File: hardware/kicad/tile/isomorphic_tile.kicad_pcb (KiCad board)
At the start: 2 copper layers, 97 x 109 mm, 135 parts, among them J101 Conn_LEFT, J102 Conn_TOP, J103 Conn_BOTTOM, J104 Conn_RIGHT, J105 BTNs_L_MSB, J106 BTNs_L_LSB, J107 BTNs_MSB, J108 BTNs_LSB, SW101 SW_Push, SW102 SW_Push, SW103 SW_Push, SW104 SW_Push, SW105 SW_Push, SW106 SW_Push, SW107 SW_Push, SW108 SW_Push, SW109 SW_Push, SW110 SW_Push, SW111 SW_Push, SW112 SW_Push, U101 74AUC2G126, U102 74AUC2G08, U103 74HC165, U104 74HC165, U105 74AHC1G04, U106 74LVC2G32, U107 74AUC2G125, U108 74LVC2G74, U109 74LS161

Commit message: KiCad: rename Italian field and footprint names
- Symbol field "Codice" (manufacturer part number) -> "MPN".
- Mouse-bite footprint "Senza-titolo" -> "MouseBite_NPTH_0.5mm".

Verified: netlist identical to rev A, switch/connector/outline
invariants OK, DRC report counts unchanged.
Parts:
- REF**10 (x4), REF**11 (x4), REF**12 (x4), REF**13 (x4), REF**14 (x4), REF**15 (x4), REF**16 (x4), REF**17 (x4), REF**18 (x4), REF**19 (x3), REF**2, REF**3 (x4), REF**4 (x4), REF**5 (x4), REF**6 (x4), REF**7 (x4), REF**8 (x4), REF**9 (x4): footprint Senza-titolo -> MouseBite_NPTH_0.5mm
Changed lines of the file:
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@@
 	(net 67 "GND_T")
 	(net 68 "VCC_T")
-	(footprint "Senza-titolo"
+	(footprint "MouseBite_NPTH_0.5mm"
 		(layer "F.Cu")
 		(at 167.9 95.75)
@@
 		(embedded_fonts no)
 	)
-	(footprint "Senza-titolo"
+	(footprint "MouseBite_NPTH_0.5mm"
 		(layer "F.Cu")
 		(at 169.5 95.75)
@@
 		(embedded_fonts no)
 	)
-	(footprint "Senza-titolo"
+	(footprint "MouseBite_NPTH_0.5mm"
 		(layer "F.Cu")
 		(at 121.3 95.75)
@@
 		(embedded_fonts no)
 	)
-	(footprint "Senza-titolo"
+	(footprint "MouseBite_NPTH_0.5mm"
 		(layer "F.Cu")
 		(at 172.9 109)
@@
 		(embedded_fonts no)
 	)
-	(footprint "Senza-titolo"
+	(footprint "MouseBite_NPTH_0.5mm"
 		(layer "F.Cu")
 		(at 170.3 95.75)
@@
 		(embedded_fonts no)
 	)
-	(footprint "Senza-titolo"
+	(footprint "MouseBite_NPTH_0.5mm"
 		(layer "F.Cu")
 		(at 172.1 109)
@@
 		(embedded_fonts no)
 	)
-	(footprint "Senza-titolo"
+	(footprint "MouseBite_NPTH_0.5mm"
 		(layer "F.Cu")
 		(at 123.7 95.75)
@@
 		)
 	)
-	(footprint "Senza-titolo"
+	(footprint "MouseBite_NPTH_0.5mm"
 		(layer "F.Cu")
 		(at 126.1 95.75)
@@
 		(embedded_fonts no)
 	)
-	(footprint "Senza-titolo"
+	(footprint "MouseBite_NPTH_0.5mm"
 		(layer "F.Cu")
 		(at 124.5 95.75)
@@
 		(embedded_fonts no)
 	)
-	(footprint "Senza-titolo"
+	(footprint "MouseBite_NPTH_0.5mm"
 		(layer "F.Cu")
 		(at 131 109)
@@
 		(embedded_fonts no)
 	)
-	(footprint "Senza-titolo"
+	(footprint "MouseBite_NPTH_0.5mm"
 		(layer "F.Cu")
 		(at 159.9 95.75)
@@
 		)
 	)
-	(footprint "Senza-titolo"
+	(footprint "MouseBite_NPTH_0.5mm"
 		(layer "F.Cu")
 		(at 128.5 95.75)
@@
 		(embedded_fonts no)
 	)
-	(footprint "Senza-titolo"
+	(footprint "MouseBite_NPTH_0.5mm"
 		(layer "F.Cu")
 		(at 164.7 95.75)
@@
 		)
 	)
-	(footprint "Senza-titolo"
+	(footprint "MouseBite_NPTH_0.5mm"
 		(layer "F.Cu")
 		(at 163.9 95.75)
@@
 		(embedded_fonts no)
 	)
-	(footprint "Senza-titolo"
+	(footprint "MouseBite_NPTH_0.5mm"
 		(layer "F.Cu")
 		(at 127.7 95.75)
@@
 		(embedded_fonts no)
 	)
-	(footprint "Senza-titolo"
+	(footprint "MouseBite_NPTH_0.5mm"
 		(layer "F.Cu")
 		(at 125.3 95.75)
@@
 		(embedded_fonts no)
 	)
-	(footprint "Senza-titolo"
+	(footprint "MouseBite_NPTH_0.5mm"
 		(layer "F.Cu")
 		(at 122.1 95.75)
@@
 		)
 	)
-	(footprint "Senza-titolo"
+	(footprint "MouseBite_NPTH_0.5mm"
 		(layer "F.Cu")
 		(at 162.5 109)
@@
 		)
 	)
-	(footprint "Senza-titolo"
+	(footprint "MouseBite_NPTH_0.5mm"
 		(layer "F.Cu")
 		(at 168.9 109)
@@
 		)
 	)
-	(footprint "Senza-titolo"
+	(footprint "MouseBite_NPTH_0.5mm"
 		(layer "F.Cu")
 		(at 165.7 109)
@@
 		(embedded_fonts no)
 	)
-	(footprint "Senza-titolo"
+	(footprint "MouseBite_NPTH_0.5mm"
 		(layer "F.Cu")
 		(at 118.9 95.75)
@@
 		)
 	)
-	(footprint "Senza-titolo"
+	(footprint "MouseBite_NPTH_0.5mm"
 		(layer "F.Cu")
 		(at 126.2 109)
@@
 		)
 	)
-	(footprint "Senza-titolo"
+	(footprint "MouseBite_NPTH_0.5mm"
 		(layer "F.Cu")
 		(at 160.1 109)
@@
 		(embedded_fonts no)
 	)
-	(footprint "Senza-titolo"
+	(footprint "MouseBite_NPTH_0.5mm"
 		(layer "F.Cu")
 		(at 127 109)
@@
 		(embedded_fonts no)
 	)
-	(footprint "Senza-titolo"
+	(footprint "MouseBite_NPTH_0.5mm"
 		(layer "F.Cu")
 		(at 129.3 95.75)
@@
 		)
 	)
-	(footprint "Senza-titolo"
+	(footprint "MouseBite_NPTH_0.5mm"
 		(layer "F.Cu")
 		(at 166.3 95.75)
@@
 		(embedded_fonts no)
 	)
-	(footprint "Senza-titolo"
+	(footprint "MouseBite_NPTH_0.5mm"
 		(layer "F.Cu")
 		(at 123.8 109)
@@
 		(embedded_fonts no)
 	)
-	(footprint "Senza-titolo"
+	(footprint "MouseBite_NPTH_0.5mm"
 		(layer "F.Cu")
 		(at 121.4 109)
@@
 		(embedded_fonts no)
 	)
-	(footprint "Senza-titolo"
+	(footprint "MouseBite_NPTH_0.5mm"
 		(layer "F.Cu")
 		(at 171.3 109)
@@
 		(embedded_fonts no)
 	)
-	(footprint "Senza-titolo"
+	(footprint "MouseBite_NPTH_0.5mm"
 		(layer "F.Cu")
 		(at 168.1 109)
@@
 		(embedded_fonts no)
 	)
-	(footprint "Senza-titolo"
+	(footprint "MouseBite_NPTH_0.5mm"
 		(layer "F.Cu")
 		(at 119.7 95.75)
@@
 		)
 	)
-	(footprint "Senza-titolo"
+	(footprint "MouseBite_NPTH_0.5mm"
 		(layer "F.Cu")
 		(at 131.8 109)
@@
 		)
 	)
-	(footprint "Senza-titolo"
+	(footprint "MouseBite_NPTH_0.5mm"
 		(layer "F.Cu")
 		(at 171.1 95.75)
@@
 		)
 	)
-	(footprint "Senza-titolo"
+	(footprint "MouseBite_NPTH_0.5mm"
 		(layer "F.Cu")
 		(at 167.3 109)
@@
 		(embedded_fonts no)
 	)
-	(footprint "Senza-titolo"
+	(footprint "MouseBite_NPTH_0.5mm"
 		(layer "F.Cu")
 		(at 122.2 109)
@@
 		)
 	)
-	(footprint "Senza-titolo"
+	(footprint "MouseBite_NPTH_0.5mm"
 		(layer "F.Cu")
 		(at 119.8 109)
@@
 		(embedded_fonts no)
 	)
-	(footprint "Senza-titolo"
+	(footprint "MouseBite_NPTH_0.5mm"
 		(layer "F.Cu")
 		(at 166.5 109)
@@
 		(embedded_fonts no)
 	)
-	(footprint "Senza-titolo"
+	(footprint "MouseBite_NPTH_0.5mm"
 		(layer "F.Cu")
 		(at 129.4 109)
@@
 		)
 	)
-	(footprint "Senza-titolo"
+	(footprint "MouseBite_NPTH_0.5mm"
 		(layer "F.Cu")
 		(at 123 109)
@@
 		)
 	)
-	(footprint "Senza-titolo"
+	(footprint "MouseBite_NPTH_0.5mm"
 		(layer "F.Cu")
 		(at 124.6 109)
@@
 		)
 	)
-	(footprint "Senza-titolo"
+	(footprint "MouseBite_NPTH_0.5mm"
 		(layer "F.Cu")
 		(at 164.1 109)
@@
 		(embedded_fonts no)
 	)
-	(footprint "Senza-titolo"
+	(footprint "MouseBite_NPTH_0.5mm"
 		(layer "F.Cu")
 		(at 162.3 95.75)
@@
 		)
 	)
-	(footprint "Senza-titolo"
+	(footprint "MouseBite_NPTH_0.5mm"
 		(layer "F.Cu")
 		(at 165.5 95.75)
@@
 		(embedded_fonts no)
 	)
-	(footprint "Senza-titolo"
+	(footprint "MouseBite_NPTH_0.5mm"
 		(layer "F.Cu")
 		(at 126.9 95.75)
@@
 		(embedded_fonts no)
 	)
-	(footprint "Senza-titolo"
+	(footprint "MouseBite_NPTH_0.5mm"
 		(layer "F.Cu")
 		(at 120.6 109)
@@
 		)
 	)
-	(footprint "Senza-titolo"
+	(footprint "MouseBite_NPTH_0.5mm"
 		(layer "F.Cu")
 		(at 160.7 95.75)
@@
 		)
 	)
-	(footprint "Senza-titolo"
+	(footprint "MouseBite_NPTH_0.5mm"
 		(layer "F.Cu")
 		(at 161.7 109)
@@
 		)
 	)
-	(footprint "Senza-titolo"
+	(footprint "MouseBite_NPTH_0.5mm"
 		(layer "F.Cu")
 		(at 172.7 95.75)
@@
 		(embedded_fonts no)
 	)
-	(footprint "Senza-titolo"
+	(footprint "MouseBite_NPTH_0.5mm"
 		(layer "F.Cu")
 		(at 125.4 109)
@@
 		(embedded_fonts no)
 	)
-	(footprint "Senza-titolo"
+	(footprint "MouseBite_NPTH_0.5mm"
 		(layer "F.Cu")
 		(at 167.1 95.75)
@@
 		(embedded_fonts no)
 	)
-	(footprint "Senza-titolo"
+	(footprint "MouseBite_NPTH_0.5mm"
 		(layer "F.Cu")
 		(at 171.9 95.75)
@@
 		)
 	)
-	(footprint "Senza-titolo"
+	(footprint "MouseBite_NPTH_0.5mm"
 		(layer "F.Cu")
 		(at 170.5 109)
@@
 		)
 	)
-	(footprint "Senza-titolo"
+	(footprint "MouseBite_NPTH_0.5mm"
 		(layer "F.Cu")
 		(at 131.7 95.75)
@@
 		(embedded_fonts no)
 	)
-	(footprint "Senza-titolo"
+	(footprint "MouseBite_NPTH_0.5mm"
 		(layer "F.Cu")
 		(at 120.5 95.75)
@@
 		)
 	)
-	(footprint "Senza-titolo"
+	(footprint "MouseBite_NPTH_0.5mm"
 		(layer "F.Cu")
 		(at 164.9 109)
@@
 		(embedded_fonts no)
 	)
-	(footprint "Senza-titolo"
+	(footprint "MouseBite_NPTH_0.5mm"
 		(layer "F.Cu")
 		(at 169.7 109)
@@
 		)
 	)
-	(footprint "Senza-titolo"
+	(footprint "MouseBite_NPTH_0.5mm"
 		(layer "F.Cu")
 		(at 127.8 109)
@@
 		)
 	)
-	(footprint "Senza-titolo"
+	(footprint "MouseBite_NPTH_0.5mm"
 		(layer "F.Cu")
 		(at 122.9 95.75)
@@
 		)
 	)
-	(footprint "Senza-titolo"
+	(footprint "MouseBite_NPTH_0.5mm"
 		(layer "F.Cu")
 		(at 119 109)
@@
 		(embedded_fonts no)
 	)
-	(footprint "Senza-titolo"
+	(footprint "MouseBite_NPTH_0.5mm"
 		(layer "F.Cu")
 		(at 130.2 109)
@@
 		)
 	)
-	(footprint "Senza-titolo"
+	(footprint "MouseBite_NPTH_0.5mm"
 		(layer "F.Cu")
 		(at 130.1 95.75)
@@
 		)
 	)
-	(footprint "Senza-titolo"
+	(footprint "MouseBite_NPTH_0.5mm"
 		(layer "F.Cu")
 		(at 130.9 95.75)
@@
 		(embedded_fonts no)
 	)
-	(footprint "Senza-titolo"
+	(footprint "MouseBite_NPTH_0.5mm"
 		(layer "F.Cu")
 		(at 163.1 95.75)
@@
 		(embedded_fonts no)
 	)
-	(footprint "Senza-titolo"
+	(footprint "MouseBite_NPTH_0.5mm"
 		(layer "F.Cu")
 		(at 128.6 109)
@@
 		(embedded_fonts no)
 	)
-	(footprint "Senza-titolo"
+	(footprint "MouseBite_NPTH_0.5mm"
 		(layer "F.Cu")
 		(at 168.7 95.75)
@@
 		(embedded_fonts no)
 	)
-	(footprint "Senza-titolo"
+	(footprint "MouseBite_NPTH_0.5mm"
 		(layer "F.Cu")
 		(at 163.3 109)
@@
 		(embedded_fonts no)
 	)
-	(footprint "Senza-titolo"
+	(footprint "MouseBite_NPTH_0.5mm"
 		(layer "F.Cu")
 		(at 160.9 109)
@@
 		)
 	)
-	(footprint "Senza-titolo"
+	(footprint "MouseBite_NPTH_0.5mm"
 		(layer "F.Cu")
 		(at 161.5 95.75)

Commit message: Rev B PCB: 4 layers, single-sided assembly, hot-swap sockets
Produced by hardware/kicad/tile/scripts/revb_pcb.py and
revb_pipeline.sh (rev-A board -> netlist update -> placement ->
Freerouting -> stitching/pours), fully reproducible.

- 4-layer 1.6 mm stack-up, In1 GND/GND_T and In2 VCC/VCC_T planes,
  Interboard net class 0.3 mm (~55 ohm), 4 mm ground stitching grid.
- Key board: Kailh MX hot-swap sockets and all resistors on B.Cu;
  switch centres unchanged (edge-trimmed socket footprint variant for
  the switches next to the stepped outline).
- Logic board: every SMD part on F.Cu; series resistors within 2.6 mm
  of their drivers; one 100 nF next to each IC.
- Fiducials (3 per board), board-only mouse bites, silkscreen revision
  v0.2, J107 courtyard margin reduced towards the SW111 socket.

Verified: DRC 0 errors, 0 unconnected, 0 schematic-parity issues;
switch/connector/outline invariants OK; SPICE tile hop as routed:
1 % overshoot (rev A: 22 %).
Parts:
- added C201: 100n, Capacitor_SMD:C_0603_1608Metric, F.Cu at (120.6, 116.8)
- added C202: 100n, Capacitor_SMD:C_0603_1608Metric, F.Cu at (137.7, 114.3)
- added C203: 100n, Capacitor_SMD:C_0603_1608Metric, F.Cu at (148.1, 119.0)
- added C204: 100n, Capacitor_SMD:C_0603_1608Metric, F.Cu at (129.3, 137.9)
- added C205: 100n, Capacitor_SMD:C_0603_1608Metric, F.Cu at (119.6, 140.3)
- added C206: 100n, Capacitor_SMD:C_0603_1608Metric, F.Cu at (133.7, 137.0)
- added C207: 100n, Capacitor_SMD:C_0603_1608Metric, F.Cu at (154.7, 130.0)
- added C208: 100n, Capacitor_SMD:C_0603_1608Metric, F.Cu at (139.6, 122.8)
- added C209: 100n, Capacitor_SMD:C_0603_1608Metric, F.Cu at (150.1, 142.8)
- added FID1: Fiducial, Fiducial:Fiducial_1mm_Mask2mm, B.Cu at (119.5, 73.2)
- added FID2: Fiducial, Fiducial:Fiducial_1mm_Mask2mm, B.Cu at (201.5, 56.0)
- added FID3: Fiducial, Fiducial:Fiducial_1mm_Mask2mm, B.Cu at (110.5, 93.0)
- added FID4: Fiducial, Fiducial:Fiducial_1mm_Mask2mm, F.Cu at (112.0, 151.0)
- added FID5: Fiducial, Fiducial:Fiducial_1mm_Mask2mm, F.Cu at (179.0, 151.0)
- added FID6: Fiducial, Fiducial:Fiducial_1mm_Mask2mm, F.Cu at (179.0, 112.0)
- added R201: 33, Resistor_SMD:R_0603_1608Metric, F.Cu at (124.1, 118.5)
- added R202: 33, Resistor_SMD:R_0603_1608Metric, F.Cu at (157.2, 127.6)
- added R203: 33, Resistor_SMD:R_0603_1608Metric, F.Cu at (133.9, 133.6)
- added R204: 33, Resistor_SMD:R_0603_1608Metric, F.Cu at (136.2, 136.1)
- added R205: 33, Resistor_SMD:R_0603_1608Metric, F.Cu at (140.2, 140.2)
- added R206: 33, Resistor_SMD:R_0603_1608Metric, F.Cu at (137.7, 137.9)
- added R207: 33, Resistor_SMD:R_0603_1608Metric, F.Cu at (139.6, 128.2)
- C101, C102: footprint Capacitor_SMD:C_0805_2012Metric_Pad1.18x1.45mm_HandSolder -> Capacitor_SMD:C_0603_1608Metric; moved to F.Cu
- C103, C104: footprint Capacitor_SMD:C_1206_3216Metric_Pad1.33x1.80mm_HandSolder -> Capacitor_SMD:C_1206_3216Metric
- C105: footprint Capacitor_THT:CP_Radial_D6.3mm_P2.50mm -> Capacitor_SMD:CP_Elec_6.3x7.7
- R101, R108: footprint Resistor_SMD:R_0805_2012Metric_Pad1.20x1.40mm_HandSolder -> Resistor_SMD:R_0603_1608Metric; moved to F.Cu
- R102, R103, R104, R105, R106, R107, R109: footprint Resistor_SMD:R_0805_2012Metric_Pad1.20x1.40mm_HandSolder -> Resistor_SMD:R_0603_1608Metric
- R110, R111, R112, R113, R114, R115, R116, R117, R118, R119, R120, R121: value 100R -> 100; footprint Resistor_SMD:R_0805_2012Metric_Pad1.20x1.40mm_HandSolder -> Resistor_SMD:R_0603_1608Metric
- R122, R123, R124, R125, R126, R127, R128, R129, R130, R131, R132, R133: footprint Resistor_SMD:R_0805_2012Metric_Pad1.20x1.40mm_HandSolder -> Resistor_SMD:R_0603_1608Metric; moved to B.Cu
- SW101, SW102, SW103, SW104, SW105, SW106, SW107, SW108, SW109, SW110, SW111, SW112: footprint Button_Switch_Keyboard:SW_Cherry_MX_1.00u_PCB -> Switch_Keyboard_Hotswap_Kailh:SW_Hotswap_Kailh_MX_1.00u_EdgeTrim
- U101: value 74AUC2G126 -> 74LVC2G126; footprint Package_SO:MSOP-8_3x3mm_P0.65mm -> Package_SO:SSOP-8_2.95x2.8mm_P0.65mm; moved to F.Cu
- U102: value 74AUC2G08 -> 74LVC2G08; footprint Package_SO:MSOP-8_3x3mm_P0.65mm -> Package_SO:SSOP-8_2.95x2.8mm_P0.65mm
- U103: value 74HC165 -> 74LVC165A
- U104: value 74HC165 -> 74LVC165A; moved to F.Cu
- U105: value 74AHC1G04 -> 74LVC1G04; footprint Package_TO_SOT_SMD:SOT-23-5_HandSoldering -> Package_TO_SOT_SMD:SOT-23-5
- U106, U108: footprint Package_SO:MSOP-8_3x3mm_P0.65mm -> Package_SO:SSOP-8_2.95x2.8mm_P0.65mm
- U107: value 74AUC2G125 -> 74LVC2G125; footprint Package_SO:MSOP-8_3x3mm_P0.65mm -> Package_SO:SSOP-8_2.95x2.8mm_P0.65mm; moved to F.Cu
- U109: value 74LS161 -> 74HC161; moved to F.Cu
- moved U104 11.6 mm to (133.8, 142.7), turned to 90 degrees
- moved U109 9.80 mm to (156.5, 145.3), turned to 90 degrees
- moved U103 9.25 mm to (154.5, 121.5), turned to 90 degrees
- moved C105 7.57 mm to (171.8, 139.5)
- moved U107 6.00 mm to (153.2, 127.2), turned to 0 degrees
- moved SW104 5.68 mm to (126.0, 70.4)
- moved SW101 5.68 mm to (155.9, 53.1)
- moved SW102 5.68 mm to (135.9, 53.1)
- moved SW103 5.68 mm to (146.0, 70.4)
- moved SW105 5.68 mm to (135.9, 87.7)
- moved SW107 5.68 mm to (195.9, 53.1)
- moved SW108 5.68 mm to (175.9, 53.1)
- moved SW109 5.68 mm to (186.0, 70.4)
- moved SW110 5.68 mm to (166.0, 70.4)
- moved SW112 5.68 mm to (155.9, 87.7)
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- renumbered REF**13 to MB1, REF**18 to MB10, REF**3 to MB11, REF**15 to MB12, REF**9 to MB13, REF**8 to MB14, REF**14 to MB15, REF**11 to MB16, REF**7 to MB17, REF**5 to MB18, REF**13 to MB19, REF**15 to MB2, REF**9 to MB20, REF**3 to MB21, REF**12 to MB22, REF**2 to MB23, REF**13 to MB24, REF**16 to MB25, REF**11 to MB26, REF**9 to MB27, REF**6 to MB28, REF**16 to MB29, REF**6 to MB3, REF**12 to MB30, REF**4 to MB31, REF**19 to MB32, REF**17 to MB33, REF**11 to MB34, REF**7 to MB35, REF**4 to MB36, REF**10 to MB37, REF**16 to MB38, REF**8 to MB39, REF**18 to MB4, REF**10 to MB40, REF**7 to MB41, REF**6 to MB42, REF**10 to MB43, REF**13 to MB44, REF**5 to MB45, REF**4 to MB46, REF**4 to MB47, REF**19 to MB48, REF**11 to MB49, REF**16 to MB5, REF**12 to MB50, REF**18 to MB51, REF**15 to MB52, REF**19 to MB53, REF**5 to MB54, REF**8 to MB55, REF**14 to MB56, REF**14 to MB57, REF**8 to MB58, REF**3 to MB59, REF**17 to MB6, REF**17 to MB60, REF**17 to MB61, REF**18 to MB62, REF**7 to MB63, REF**15 to MB64, REF**14 to MB65, REF**6 to MB66, REF**3 to MB67, REF**5 to MB68, REF**9 to MB7, REF**12 to MB8, REF**10 to MB9
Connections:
- J102 pad 6: /tile/L_latch -> /tile/T_latch
- J104 pad 3: /tile/B_data -> /tile/R_data
- U101 pad 6: /tile/L_clk -> /tile/L_clk_drv
- U102 pad 1: /tile/B_data -> /tile/data_drv
- U104 pad 9: /tile/B_data -> /tile/data_drv
- U105 pad 2: /tile/L_latch -> /tile/latch_drv
- U106 pad 5: /tile/B_W -> /tile/B_W_drv
- U106 pad 7: /tile/L_latch -> /tile/latch_drv
- U107 pad 6: /tile/T_clk -> /tile/T_clk_drv
- U108 pad 5: /tile/B_W -> /tile/B_W_drv
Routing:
- net GND: track 212.3 -> 34.0 mm, vias 2 -> 123
- net VCC: track 208.8 -> 32.1 mm, vias 4 -> 32
- net /tile/B_data: track 86.7 -> 12.6 mm, vias 2 -> 0
- net /tile/L_latch: track 82.8 -> 22.5 mm, vias 3 -> 1
- net /tile/data_drv: track 0.00 -> 53.2 mm, vias 0 -> 3
- net /tile/R_data: track 0.00 -> 52.8 mm, vias 0 -> 1
- net /tile/B_first: track 36.0 -> 88.1 mm, vias 0 -> 1
- net /tile/T_latch: track 0.00 -> 36.6 mm, vias 0 -> 4
- net /tile/T_data: track 13.7 -> 45.1 mm, vias 0 -> 1
- net /tile/latch_drv: track 0.00 -> 29.7 mm
- net Net-(U103-Q7): track 15.4 -> 45.0 mm, vias 1 -> 2
- net Net-(U103-DS): track 41.0 -> 63.9 mm, vias 1 -> 4
- net VCC_T: track 39.3 -> 18.6 mm, vias 0 -> 12
- net Net-(R110-Pad1): track 12.2 -> 32.1 mm
- net /tile/counter/~{rst}: track 75.4 -> 94.7 mm, vias 3 -> 2
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- added copper zone on B.Cu, net GND
- added copper zone on In1.Cu, net GND
- added copper zone on B.Cu, net GND_T
- added copper zone on In1.Cu, net GND_T
- added copper zone on In2.Cu, net VCC
- added copper zone on In2.Cu, net VCC_T
- removed copper zone on B.Cu, net VCC
- removed copper zone on B.Cu, net VCC_T
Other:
- copper layers 2 -> 4
- board text added: "TORTIRE v0.2 (rev B)"
- board text added: "TORTIRE v0.2 (rev B) Orturano Labs"
- board text removed: "TORTIRE v0.1"
- board text removed: "TORTIRE v0.1 Orturano Labs"

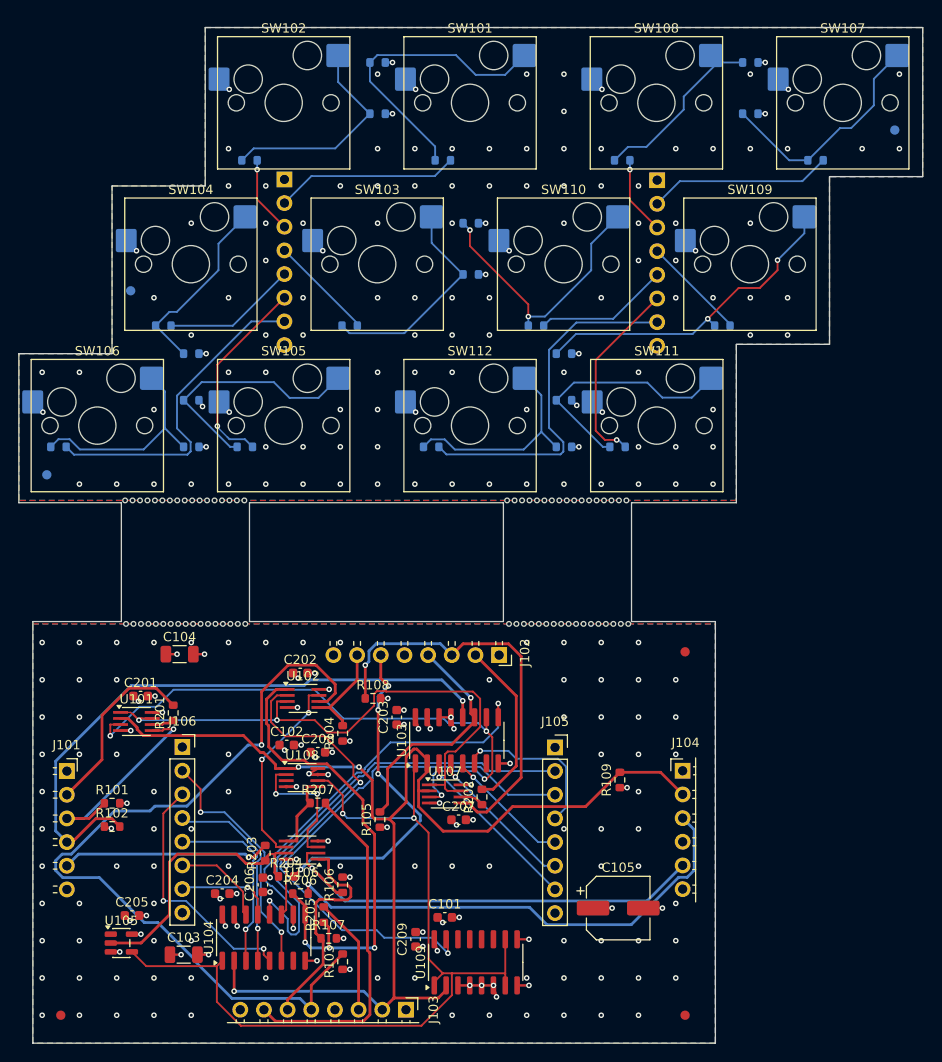
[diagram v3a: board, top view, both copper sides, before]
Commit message: Rev B: keep vias off SMD pads; add KiCadRoutingTools as optional router
- Fan-out vias now keep >= 0.35 mm of mask to their own pad and treat
  same-net SMD pads as obstacles; the previous layout had 83 vias
  within 0.2 mm of an SMD pad (solder wicking risk), found by
  KiCadRoutingTools' fab check. New tools/scripts/check_via_in_pad.py
  runs in the pipeline and in production.sh (0 on the new layout).
- revb_pipeline.sh: ROUTER=freerouting (default) or ROUTER=krt
  (KiCadRoutingTools in a rootless container, strict options);
  revb_pcb.py gains --finish and --export-dsn.
- Regenerated rev-B board: DRC 0 errors / 0 unconnected / 0 parity,
  invariants OK.
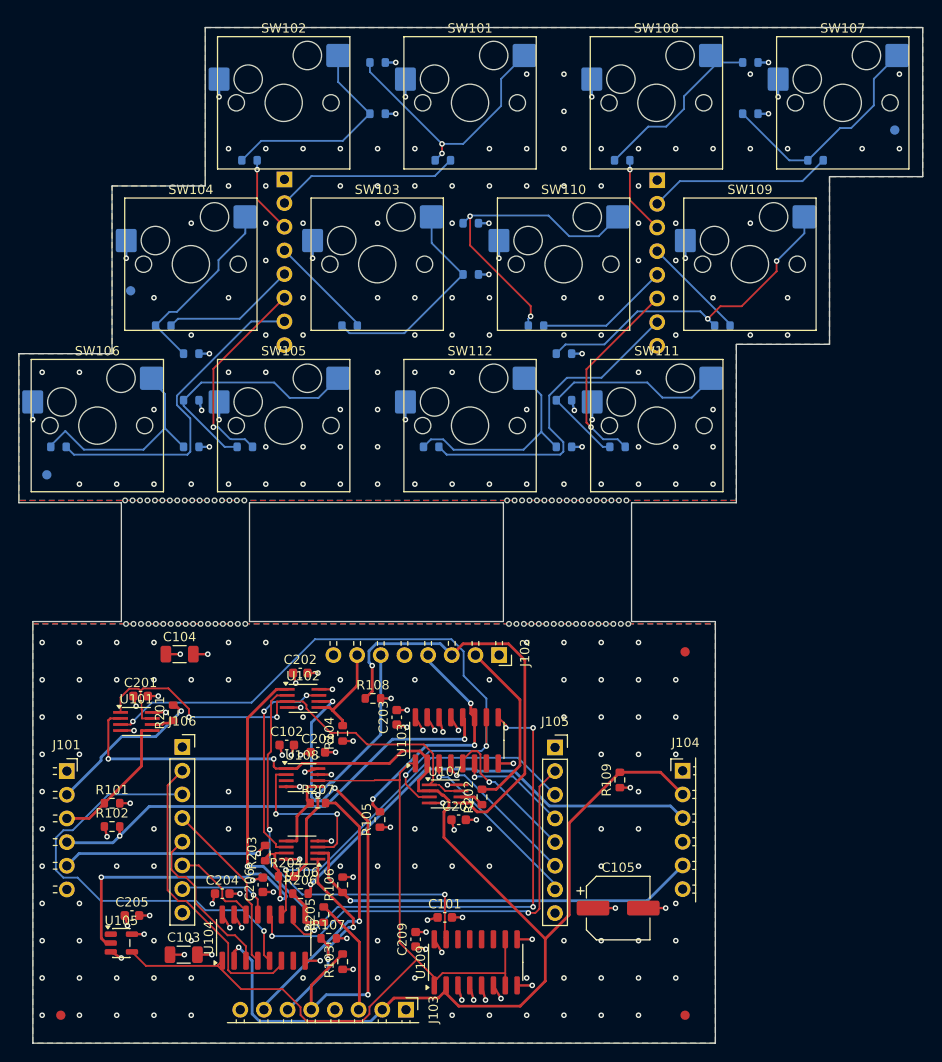
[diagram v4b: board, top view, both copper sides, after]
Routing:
- net /tile/B_first: track 88.1 -> 53.7 mm, vias 1 -> 3
- net /tile/BTNs_L1: track 26.7 -> 47.5 mm, vias 2 -> 1
- net /tile/L_endrow: track 66.2 -> 50.8 mm, vias 1 -> 2
- net /tile/data_drv: track 53.2 -> 37.9 mm, vias 3 -> 2
- net /tile/B_clk: track 133.9 -> 147.3 mm
- net GND: track 34.0 -> 45.6 mm, vias 123 -> 124
- net VCC: track 32.1 -> 43.3 mm
- net Net-(U101-Pad1): track 62.2 -> 53.1 mm
- net Net-(U109-Tc): track 53.4 -> 44.6 mm
- net /tile/T_latch: track 36.6 -> 27.8 mm, vias 4 -> 1
- net /tile/counter/~{rst}: track 94.7 -> 86.1 mm, vias 2 -> 0
- net /tile/latch_drv: track 29.7 -> 37.3 mm, vias 0 -> 2
- net /tile/B_W: track 36.9 -> 29.3 mm, vias 0 -> 1
- net /tile/L_data: track 22.5 -> 15.3 mm, vias 1 -> 0
- net Net-(U103-Q7): track 45.0 -> 52.0 mm, vias 2 -> 4
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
